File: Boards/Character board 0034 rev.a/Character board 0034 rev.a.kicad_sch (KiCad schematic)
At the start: 64 parts, among them J1 card edge, J2 character connector, Q1 2N6125, U1 2.2K, U1 6821, U13 7406, U14 74LS42, U15 LM741, U16 AH5012, U2 2.2K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

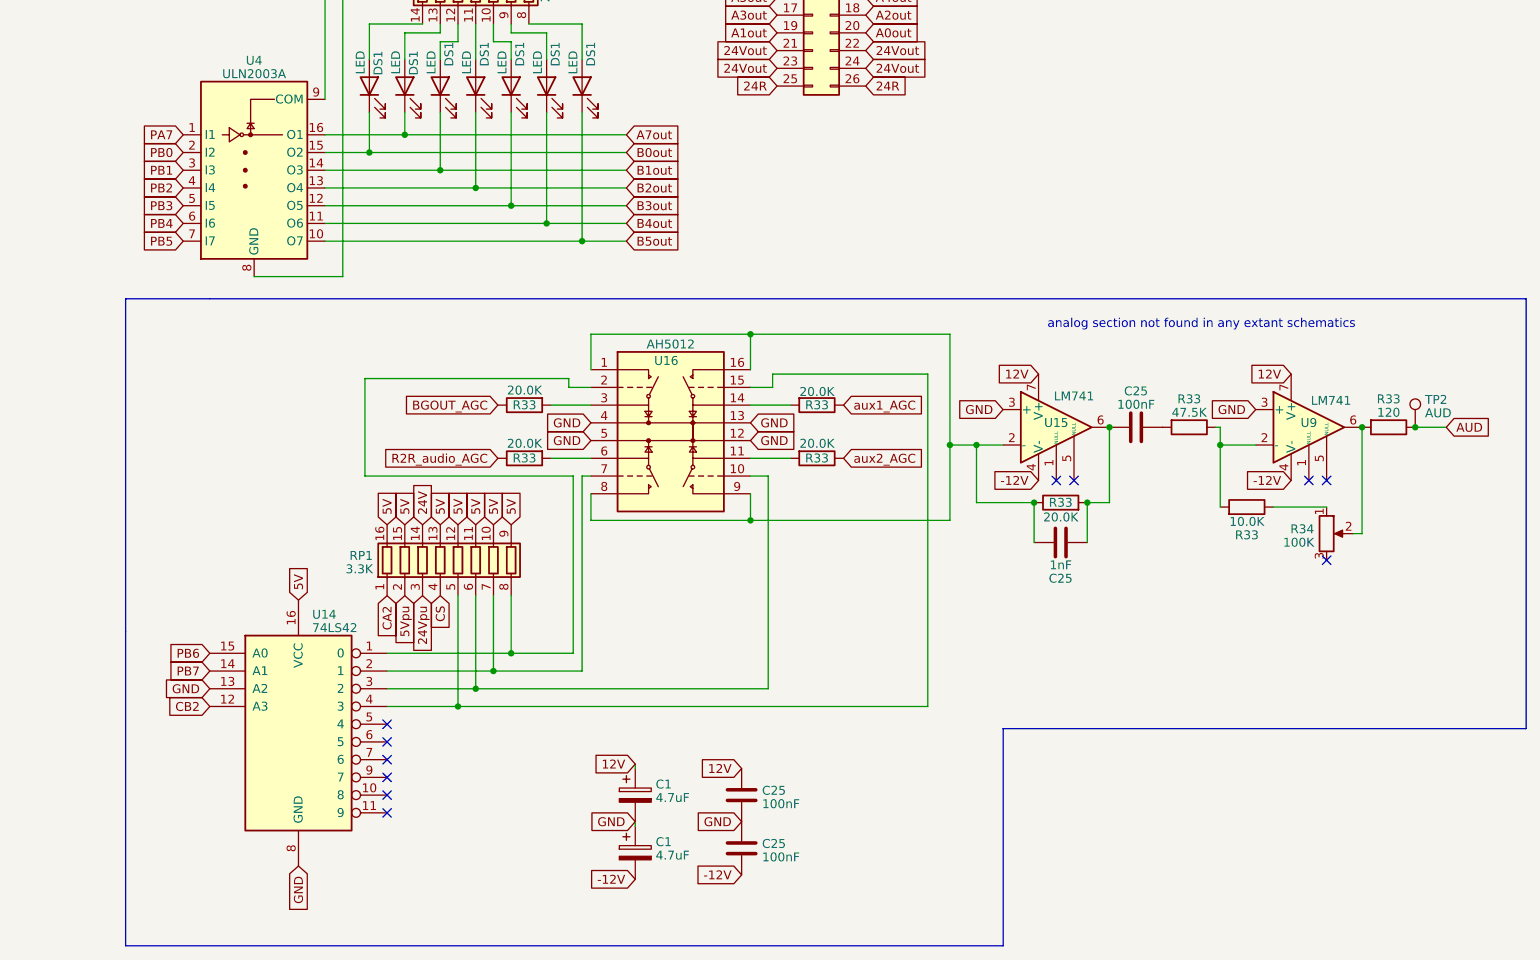
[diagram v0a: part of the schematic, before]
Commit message: updated boards to have correct logos
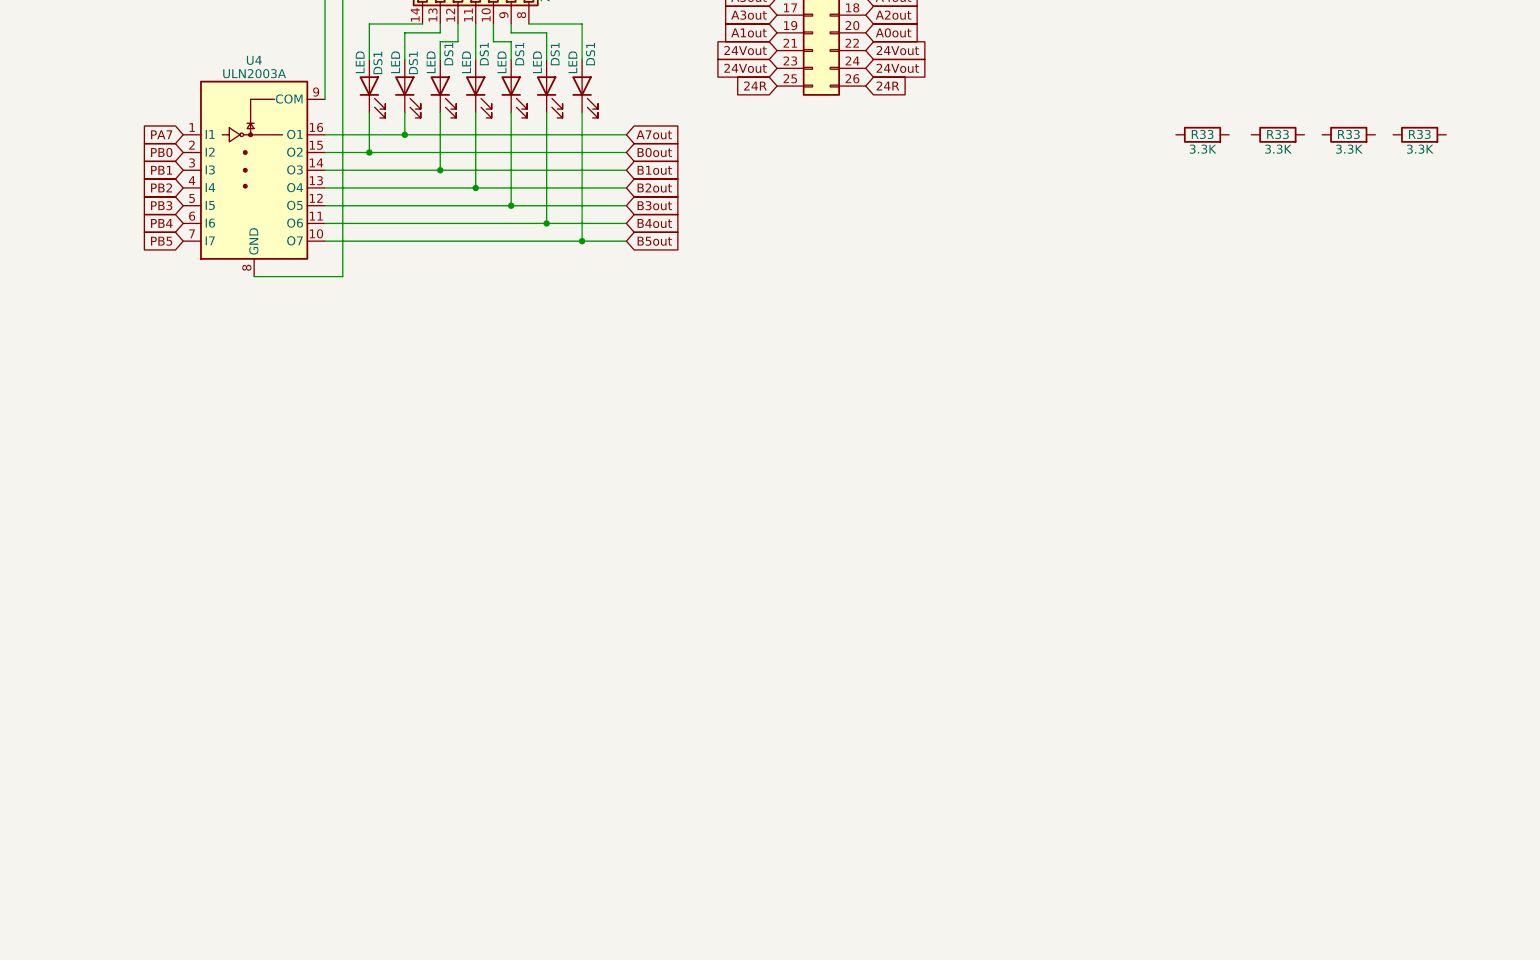
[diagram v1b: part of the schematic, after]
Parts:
- removed C1 (x2): 4.7uF, Evan's parts:CP_Radial_Tantal_D4mm_P3.81mm, symbol Device:C_Polarized
- removed C25 (x3): 100nF, Capacitor_THT:C_Rect_L7.0mm_W2.5mm_P5.00mm, symbol Device:C
- removed C25: 1nF, Capacitor_THT:C_Rect_L9.0mm_W2.7mm_P7.50mm_MKT, symbol Device:C
- removed R33: 47.5K, Resistor_THT:R_Axial_DIN0309_L9.0mm_D3.2mm_P12.70mm_Horizontal, symbol Device:R
- removed R33 (x5): 20.0K, Resistor_THT:R_Axial_DIN0309_L9.0mm_D3.2mm_P12.70mm_Horizontal, symbol Device:R
- removed R33: 10.0K, Resistor_THT:R_Axial_DIN0309_L9.0mm_D3.2mm_P12.70mm_Horizontal, symbol Device:R
- removed R33: 120, Resistor_THT:R_Axial_DIN0309_L9.0mm_D3.2mm_P12.70mm_Horizontal, symbol Device:R
- removed R34: 100K, Potentiometer_THT:Potentiometer_Bourns_3005_Horizontal, symbol Device:R_Potentiometer
- removed RP1: 3.3K, Package_DIP:DIP-16_W7.62mm, symbol Device:R_Pack08
- removed TP2: AUD, TestPoint:TestPoint_Plated_Hole_D3.0mm, symbol Connector:TestPoint
- removed U14: 74LS42, Package_DIP:DIP-16_W7.62mm, symbol 74xx:74LS42
- removed U15, U9: LM741, Package_DIP:DIP-8_W7.62mm, symbol Amplifier_Operational:LM741
- removed U16: AH5012, Package_DIP:DIP-16_W7.62mm, symbol Evan's parts:AH5012
- added R33 (x4): 3.3K, Resistor_THT:R_Axial_DIN0309_L9.0mm_D3.2mm_P12.70mm_Horizontal, symbol Device:R
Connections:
- no-connect marks 92 -> 81
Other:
- note removed: "analog section not found in any extant schematics"

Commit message: completed 0034 rev a
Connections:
- net 24Vpu is gone; now on an unnamed net: Q1.1 (B), R33.1
- net 5Vpu is gone; now on an unnamed net: U13.11, U13.12
- net AUD is gone; now on net GND: J2.2 (Pin_2)
- net CA2 is gone; now on an unnamed net: U1.39 (CA2), U13.13
- net CS is gone; now on an unnamed net: U1.22 (CS0), U1.24 (CS1)
- net 24V: now also R33.2
- net 5V: now also R33.1, R33.2, R33.2
- net A4out: now also DS1.1 (K); no longer DS1.1 (K)
- net A6out: now also DS1.1 (K); no longer DS1.1 (K)
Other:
- note added: "AUD on older cards"
- moved on the sheet: C1, C25, CR1, DS1, F1, J1, J2, Q1, R33, RP1, TP2, U1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

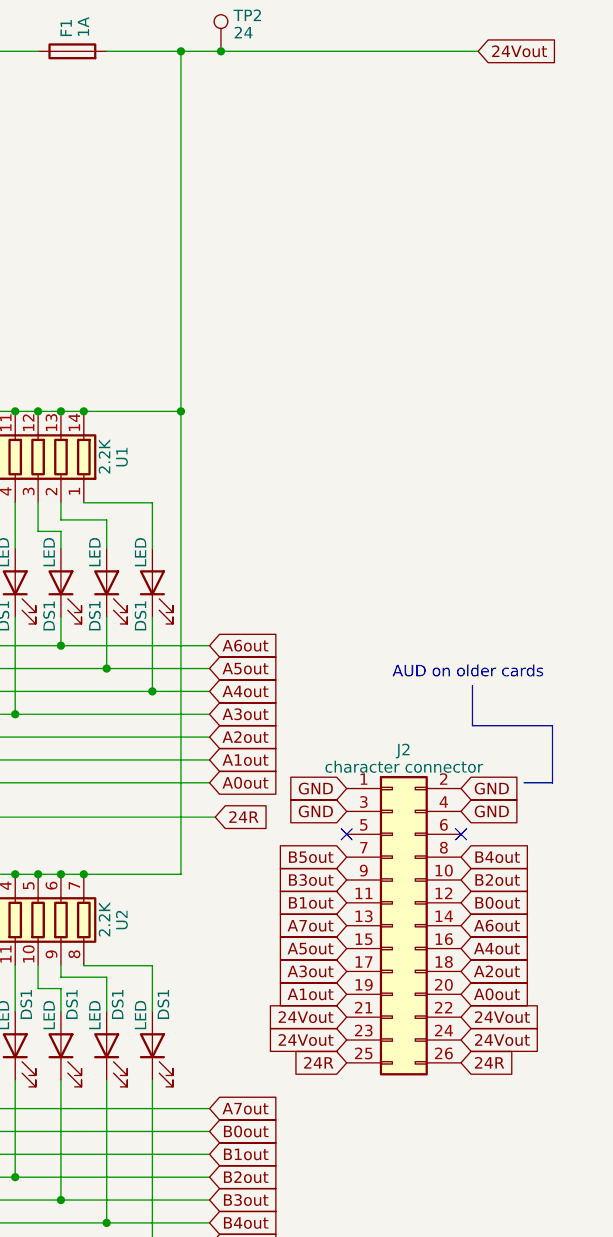
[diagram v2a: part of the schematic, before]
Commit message: finish light board rev.a, rename files, add renders and schematics, move pictures
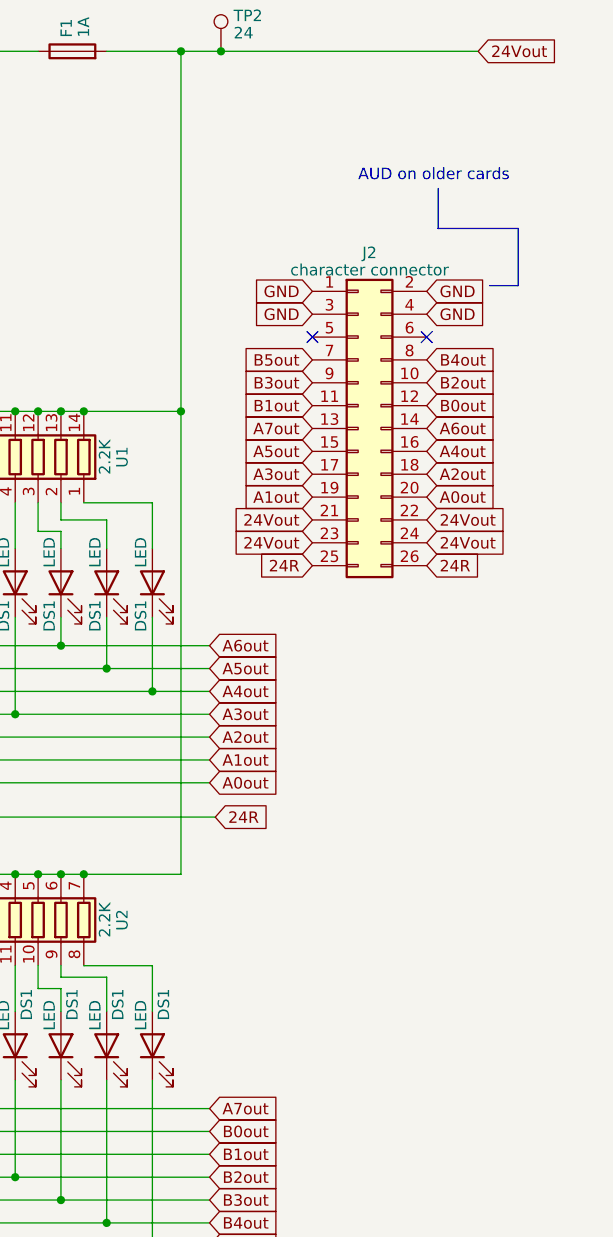
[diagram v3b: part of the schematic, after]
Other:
- moved on the sheet: J2
